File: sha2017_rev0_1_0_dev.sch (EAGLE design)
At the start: 195 parts, among them IC1 CP210X_USB_UART, IC2 AP7215, IC3 ESP32WROOM32, IC4 MCP73833, IC5 FXL6408, IC6 CPT112, Q1 MOSFET-PCHANNEL, Q2 MMBT2222A, Q3 MMBT2222A, Q4 MMBT2222A, Q5 MMBT2222A, Q6 SI1304 BDL, Q7 MMBT2222A, Q8 MOSFET-PCHANNEL, T1 SI2301DS, X1 JST-PH3, X2 2908-05WB-MG

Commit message: fixed designators
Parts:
- removed SJ3: JUMPER-PAD-2-NC_BY_TRACE, SparkFun-Passives:JUMPER-PAD-2-NC_BY_TRACE
- removed U$26, U$27, U$28: VIA, badge:VIA
- added $$U$1, $$U$2, $$U$3: VIA, badge:VIA
- added SJ1: JUMPER-PAD-2-NC_BY_TRACE, SparkFun-Passives:JUMPER-PAD-2-NC_BY_TRACE
- C10: PARTNO (none) -> GRM188R71H104KA93D
- C12: value 4u7/16V -> 100n; device rcl:C-EUC0805 -> rcl:C-EUC0603; PARTNO GRM21BR61C475KA88K -> (none)
- C13: OC_FARNELL unknown -> (none); PARTNO (none) -> GRM188R71H104KA93D
- C15: value 4u7/16V -> 100n; device rcl:C-EUC0805 -> rcl:C-EUC0603; OC_FARNELL (none) -> unknown; PARTNO GRM21BR61C475KA88K -> (none)
- C16, C29: value 1u -> 4u7/16V; device rcl:C-EUC0603 -> rcl:C-EUC0805; PARTNO GRM188R61E105KA12D -> GRM21BR61C475KA88K
- C19: value 100n -> 4u7/16V; device rcl:C-EUC0603 -> rcl:C-EUC0805; PARTNO GRM188R71H104KA93D -> GRM21BR61C475KA88K
- C20, C30: value 10uF -> 1u; device rcl:C-EUC0805K -> rcl:C-EUC0603; PARTNO (none) -> GRM188R61E105KA12D
- C21: value 100nF -> 100n; device rcl:C-EUC0402K -> rcl:C-EUC0603; PARTNO (none) -> GRM188R71H104KA93D
- C22, C32: value 1u -> 10uF; device rcl:C-EUC0603 -> rcl:C-EUC0805K; PARTNO GRM188R61E105KA12D -> (none)
- C23: value 4u7/16V -> 100nF; device rcl:C-EUC0805 -> rcl:C-EUC0402K; PARTNO GRM21BR61C475KA88K -> (none)
- C24, C35: value 100n -> 1u; PARTNO GRM188R71H104KA93D -> GRM188R61E105KA12D
- C25: value (none) -> 4u7/16V; device rcl:C-EUC0603 -> rcl:C-EUC0805; OC_FARNELL unknown -> (none); PARTNO (none) -> GRM21BR61C475KA88K
- C26, C37: value (none) -> 100n; OC_FARNELL unknown -> (none); PARTNO (none) -> GRM188R71H104KA93D
- C27: value 4u7/16V -> (none); device rcl:C-EUC0805 -> rcl:C-EUC0603; OC_FARNELL (none) -> unknown; PARTNO GRM21BR61C475KA88K -> (none)
- C28: value 1u -> (none); OC_FARNELL (none) -> unknown; PARTNO GRM188R61E105KA12D -> (none)
- C3: value 4u7/16V -> 100n; device 00ralf:C0603-DASHES -> rcl:C-EUC0603
- C36: value 4u7/16V -> 1u; device 00ralf:C0603-DASHES -> rcl:C-EUC0603; PARTNO (none) -> GRM188R61E105KA12D
- C38: value 100n -> 4u7/16V; device rcl:C-EUC0603 -> 00ralf:C0603-DASHES; PARTNO GRM188R71H104KA93D -> (none)
- C39: value 100n -> (none); OC_FARNELL (none) -> unknown; PARTNO GRM188R71H104KA93D -> (none)
- C4: value 100n -> 4u7/16V; device rcl:C-EUC0603 -> 00ralf:C0603-DASHES
- C7: value 4u7/16V -> 100n; device rcl:C-EUC0805 -> rcl:C-EUC0603; PARTNO GRM21BR61C475KA88K -> GRM188R71H104KA93D
- C8: value 100n -> 4u7/16V; device rcl:C-EUC0603 -> rcl:C-EUC0805; OC_FARNELL unknown -> (none); PARTNO (none) -> GRM21BR61C475KA88K
- C9: OC_FARNELL (none) -> unknown; PARTNO GRM188R71H104KA93D -> (none)
- D2: PARTNO (none) -> BAT20JFILM
- D3: value Yellow -> NSVR0320MW2T1G; device SparkFun-LED:LED0603 -> SparkFun-DiscreteSemi:BAT20JFILM
- D4: value RED -> Yellow
- D5: value green -> RED
- D6: value NSVR0320MW2T1G -> green; device SparkFun-DiscreteSemi:BAT20JFILM -> SparkFun-LED:LED0603; PARTNO BAT20JFILM -> (none)
- R1: value 10R -> 10k
- R10: device rcl:R-EU_R0603 -> 00ralf:R0603-DASHES; PARTNO ERJ-3GEYJ103V -> (none)
- R11, R9: value 1k -> 10k; device rcl:R-EU_R0603 -> 00ralf:R0603-DASHES; PARTNO ERJ-3GEYJ102V -> (none)
- R12, R14: value 10k -> 1k; PARTNO ERJ-3GEYJ103V -> ERJ-3GEYJ102V
- R15: value 5R -> 10k; device 00ralf:R0603-DASHES -> rcl:R-EU_R0603; PARTNO ERJ-3GEYJ5R1V -> ERJ-3GEYJ103V
- R16: value 100k -> 10k; PARTNO (none) -> ERJ-3GEYJ103V
- R17, R5: value 220k -> 10k; device rcl:R-EU_R0603 -> 00ralf:R0603-DASHES
- R18: OC_FARNELL unknown -> (none)
- R19: value 470R -> 5R; device rcl:R-EU_R0603 -> 00ralf:R0603-DASHES; OC_FARNELL unknown -> (none); PARTNO ERJ-3GEYJ103V -> ERJ-3GEYJ5R1V
- R2: value 1k -> 10R; device rcl:R-EU_R0603 -> 00ralf:R0603-DASHES; PARTNO ERJ-3GEYJ102V -> (none)
- R20: value 470R -> 100k; OC_FARNELL unknown -> (none); PARTNO ERJ-3GEYJ103V -> (none)
- R21, R7: value 10k -> 220k; device 00ralf:R0603-DASHES -> rcl:R-EU_R0603
- R22, R33: device 00ralf:R0603-DASHES -> rcl:R-EU_R0603; OC_FARNELL (none) -> unknown; PARTNO (none) -> ERJ-3GEYJ103V
- R23: value 2.2k -> 470R; OC_FARNELL (none) -> unknown; PARTNO (none) -> ERJ-3GEYJ103V
- R24: value 1k -> 470R; OC_FARNELL (none) -> unknown; PARTNO (none) -> ERJ-3GEYJ103V
- R25: value 100k -> 10k; device rcl:R-EU_R0603 -> 00ralf:R0603-DASHES; PARTNO CRCW0603100KFKEA -> (none)
- R26: value 150k -> 10k; device rcl:R-EU_R0603 -> 00ralf:R0603-DASHES
- R27: device rcl:R-EU_R0603 -> 00ralf:R0603-DASHES; OC_FARNELL unknown -> (none); PARTNO ERJ-3GEYJ103V -> (none)
- R28: value 1k -> 10k; device rcl:R-EU_R0603 -> 00ralf:R0603-DASHES
- R29: value 10k -> 2.2k; device 00ralf:R0603-DASHES -> rcl:R-EU_R0603
- R3: value 10k -> 1k; PARTNO (none) -> ERJ-3GEYJ102V
- R30, R34: value 10k -> 1k; device 00ralf:R0603-DASHES -> rcl:R-EU_R0603
- R31: value 10k -> 100k; device 00ralf:R0603-DASHES -> rcl:R-EU_R0603; PARTNO (none) -> CRCW0603100KFKEA
- R32: value 10k -> 150k; device 00ralf:R0603-DASHES -> rcl:R-EU_R0603
- R4: value 100k -> 10k
- R6: value 10k -> 100k; device 00ralf:R0603-DASHES -> rcl:R-EU_R0603
- X1: value JST-PH3 -> 2908-05WB-MG; device badge:JST-PH3 -> con-3m:2908-05WB-MG; PARTNO (none) -> 2908-05WB-MG
- X2: value 2908-05WB-MG -> (none); device con-3m:2908-05WB-MG -> EAGLE-BOARD-TO-BOARD_CONNECTORS-rev16c:610X12243021; PARTNO 2908-05WB-MG -> (none)
- X3: value (none) -> JST-PH3; device EAGLE-BOARD-TO-BOARD_CONNECTORS-rev16c:610X12243021 -> badge:JST-PH3
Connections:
- net +3V3: now also C11.1, C16.1, C21.1, C25.1, C26.1, C29.1, C36.1, C6.1, R1.2, R16.2, R17.2, R22.1, R23.1, R24.1, R25.2, R26.2, R31.1, R33.1, R5.2, R8.2; no longer C14.1, C17.1, C23.1, C24.1, C27.1, C34.1, C37.1, C38.1, R13.2, R18.1, R19.1, R20.1, R22.2, R25.1, R27.1, R29.2, R30.2, R31.2, R32.2, R33.2
- net +5V: now also C10.1, C22.2, C23.2, C8.1, D3.A, R4.2, R7.2; no longer C20.2, C21.2, C7.1, C9.1, D2.A, R3.2, R5.2
- net 3V3_SWITCHED: now also C37.1, C38.1, X1.VCC, X2.1; no longer C35.1, C36.1, X2.VCC, X3.1
- net ESP32_!RESET: now also R22.2; no longer R18.2
- net ESP32_FLASH: now also D2.C, R16.1; no longer D9.C, R13.1
- net ESP32_RX: now also D4.C; no longer D3.C
- net ESP32_TX: now also D5.C; no longer D4.C
- net EXTIO-0: now also X2.10; no longer X3.10
- net EXTIO-1: now also X2.9; no longer X3.9
- net EXTIO-2: now also X2.8; no longer X3.8
- net EXTIO-3: now also X2.4; no longer X3.4
- net EXTIO-4: now also X2.3; no longer X3.3
- net EXTIO-5: now also X2.2; no longer X3.2
- net GND: now also $$U$1.P$1, $$U$2.P$1, $$U$3.P$1, C10.2, C12.1, C16.2, C21.2, C22.1, C23.1, C25.2, C26.2, C27.1, C29.2, C3.1, C34.1, C35.1, C4.2, D7.C, R19.2, R20.1, R29.1, R32.1, R6.1, X1.GND, X1.SHIELD@2, X1.SHIELD@3, X1.SHIELD@4, X2.12, X32.1; no longer C10.1, C12.2, C16.1, C21.1, C23.2, C24.2, C25.1, C26.1, C27.2, C29.1, C3.2, C34.2, C35.2, C4.1, D5.C, R15.2, R16.1, R23.1, R26.1, R3.1, U$26.P$1, U$27.P$1, U$28.P$1, X12.1, X2.GND, X2.SHIELD@2, X2.SHIELD@3, X2.SHIELD@4, X3.12
- net I2C_SCL: now also R24.2, X2.7; no longer R20.2, X3.7
- net I2C_SDA: now also R23.2, X2.6; no longer R19.2, X3.6
- net N$10: now also R15.1; no longer R12.1
- net N$11: now also R18.1; no longer R14.1
- net N$13: now also R15.2; no longer R12.2
- net N$14: now also R18.2; no longer R14.2
- net N$15: now also R27.2; no longer R21.2
- net N$17: now also R28.1; no longer R22.1
- net N$18: now also R2.1; no longer R1.1
- net N$20: now also SJ2.2, X1.DO; no longer SJ3.2, X2.DO
- net N$22: now also C24.1, D7.A, D8.C; no longer C22.1, D6.A, D7.C
- net N$23: now also C24.2, D9.A; no longer C22.2, D8.A
- net N$26: now also D6.A, R12.1; no longer D5.A, R9.1
- net N$27: now also D4.A, R3.1; no longer D3.A, R2.1
- net N$28: now also D5.A, R14.1; no longer D4.A, R11.1
- net N$42: now also C27.2; no longer C25.2
- net N$43: now also C28.2; no longer C26.2
- net N$45: now also R11.1; no longer R8.1
- net N$46: now also R29.2; no longer R23.2
- net N$47: now also R30.2; no longer R24.2
- net N$48: now also R30.1, R32.2, X31.1; no longer R24.1, R26.2, X11.1
- net N$49: now also C32.2, X33.1; no longer C30.2, X13.1
- net N$52: now also R10.2; no longer R7.2
- net N$53: now also R9.1; no longer R6.1
- net N$59: now also R33.2; no longer R27.2
- net N$61: now also R34.1; no longer R28.1
- net N$8: now also R13.2; no longer R10.2
- net PREVGH: now also C30.2, D9.C; no longer C28.2, D8.C
- net PREVGL: now also C34.2, D8.A; no longer C32.2, D7.A
- net RESE: now also R19.1; no longer R15.1
- net SD_CD: now also R31.2, X1.SHIELD@1; no longer R25.2, X2.SHIELD@1
- net SD_CLK: now also R25.1, X1.SCK; no longer R32.1, X2.SCK
- net SD_CMD: now also R8.1, X1.DI; no longer R31.1, X2.DI
- net SD_DATA0: now also D2.A, R5.1, SJ2.1; no longer D9.A, R33.1, SJ3.1
- net SD_DATA1: now also R1.1, X1.RSV; no longer R34.1, X2.RSV
- net SD_DATA2: now also SJ1.1; no longer SJ2.1
- net SD_DATA2_OUT: now also R26.1, SJ1.2, X1.NC; no longer R29.1, SJ2.2, X2.NC
- net SD_DATA3: now also R17.1, X1.CS; no longer R30.1, X2.CS
- net VBAT: now also R21.2; no longer R17.2
- net VBAT_SENSE: now also C15.1, R20.2, R21.1; no longer C13.1, R16.2, R17.1
- net VCC: now also C13.1, C14.1, C17.1, D3.C, R2.2, R9.2; no longer C11.1, C12.1, C15.1, D2.C, R1.2, R6.2
- net VCOM: now also C35.2; no longer C33.2
- net VDD: now also C7.1, R12.2, R13.1, R14.2, R3.2; no longer C6.1, R10.1, R11.2, R2.2, R9.2
- net VGH: now also C20.2; no longer C18.2
- net VGL: now also C18.2; no longer C16.2
- net VIBRATOR: now also R11.2; no longer R8.2
- net VSH: now also C31.2; no longer C29.2
- net VSL: now also C33.2; no longer C31.2
- net VUSB_SENSE: now also C9.1, R6.2, R7.1; no longer C8.1, R4.2, R5.1
- net WS2812_DATA_OUT: now also X2.5; no longer X3.5
- net WS2812_POWER: now also C12.2, C3.2, C4.1, X2.11; no longer C10.2, C3.1, C4.2, X3.11
- net WS2812_POWER_EN: now also R10.1, R27.1; no longer R21.1, R7.1

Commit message: some small fixes
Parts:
- renumbered J1 to X4
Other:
- note added: "Port Expander"
- note added: "Spezial Vias with thermals (hack)"
- note added: "Touch Controller"
- moved on the sheet: C39, IC5, R23, R24, R33, TP102, TP109, TP111, TP113, TP114, TP115, TP116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

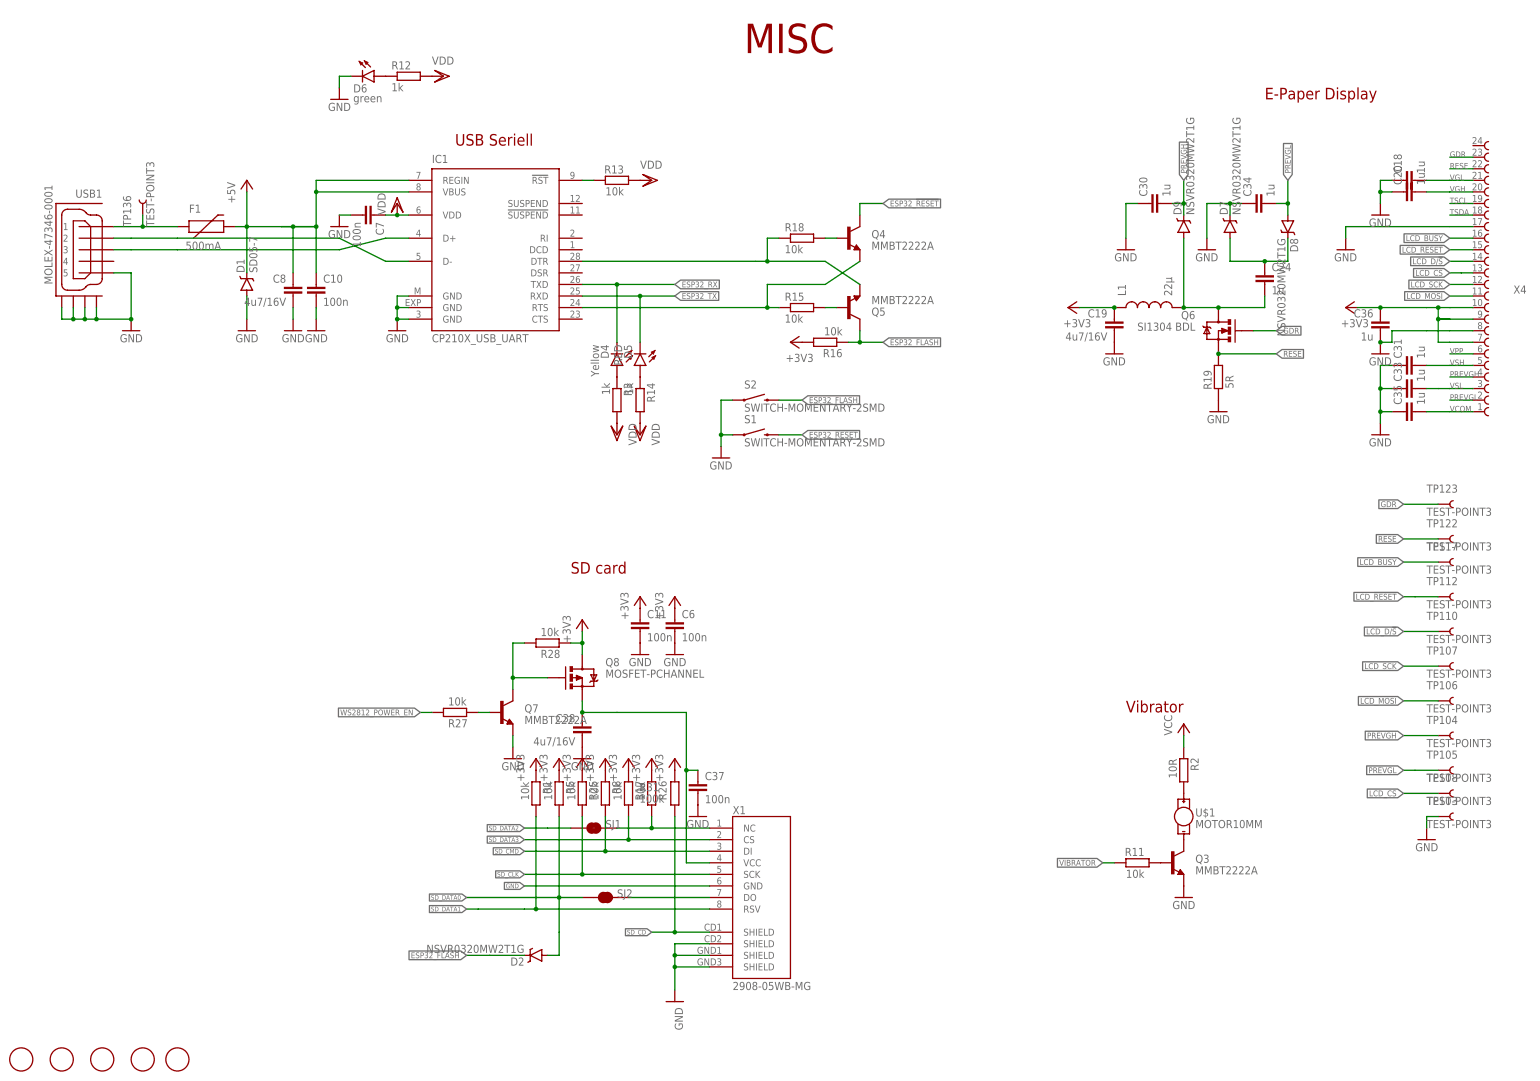
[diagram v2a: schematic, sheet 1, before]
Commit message: cleanup an Testpoint marking
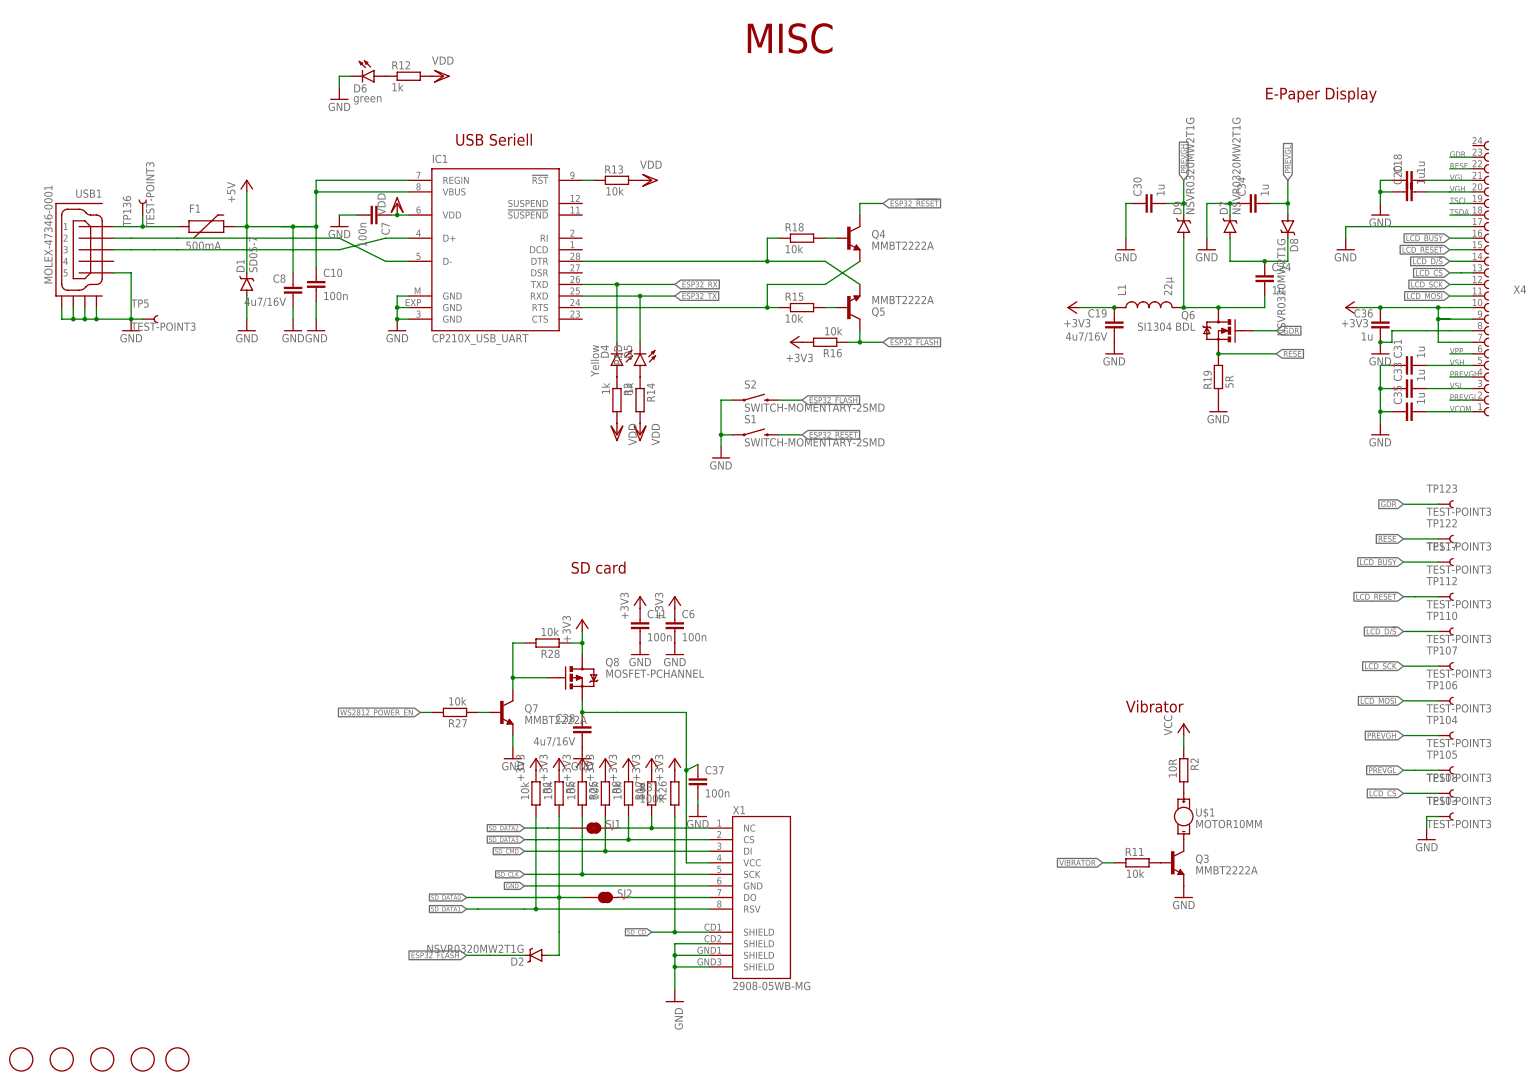
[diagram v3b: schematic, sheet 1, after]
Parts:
- added TP5: TEST-POINT3, SparkFun-Passives:TEST-POINT3
- $$U$1, $$U$2, $$U$3, $$U$7, $$U$8, $$U$9, FD1, FD2, FD3, FD4, FD5, TB100, TB101, TB102, TB103, TB104, TP1, TP100, TP101, TP102, TP103, TP104, TP105, TP106, TP107, TP108, TP109, TP110, TP111, TP112, TP113, TP114, TP115, TP116, TP117, TP118, TP119, TP120, TP121, TP122, TP123, TP124, TP125, TP126, TP127, TP128, TP129, TP130, TP131, TP132, TP133, TP134, TP135, TP136, TP137, TP138, TP139, TP2, U$10, U$11, U$12, U$13, U$14, U$15, U$16, U$17, U$18, U$19, U$2, U$20, U$21, U$22, U$23, U$24, U$25, U$3, U$4, U$5, U$6: PARTNO (none) -> NAP
- C1, C12, C15, C2, C3, C5, C9: device rcl:C-EUC0603 -> sha2017_rev0_1_0_dev:C0603-DASHES; PARTNO (none) -> GRM188R71H104KA93D
- C10, C11, C13, C18, C20, C21, C24, C26, C30, C31, C33, C34, C35, C36, C37, C39, C40, C6, C7: device rcl:C-EUC0603 -> sha2017_rev0_1_0_dev:C0603-DASHES
- C22, C32: value 10uF -> 10u
- C23: value 100nF -> 100n; device rcl:C-EUC0402K -> sha2017_rev0_1_0_dev:C0603-DASHES; PARTNO (none) -> GRM188R71H104KA93D
- C27, C28: value (none) -> 100n; device rcl:C-EUC0603 -> sha2017_rev0_1_0_dev:C0603-DASHES
- D100, D101, D102, D103, D104: PARTNO (none) -> WS2812B
- D3: PARTNO (none) -> BAT20JFILM
- F2: PARTNO (none) -> 0ZCJ0025FF2E
- Q2, Q3, Q7: PARTNO (none) -> BC817-25,215
- R1, R10, R11, R27, R28, R5, R8, R9: PARTNO (none) -> ERJ-3GEYJ103V
- R12, R13, R14, R15, R16, R18, R21, R22, R23, R24, R29, R3, R31, R32, R33, R7: device rcl:R-EU_R0603 -> sha2017_rev0_1_0_dev:R0603-DASHES
- R17, R25, R26: device 00ralf:R0603-DASHES -> sha2017_rev0_1_0_dev:R0603-DASHES; PARTNO (none) -> ERJ-3GEYJ103V
- R19: device 00ralf:R0603-DASHES -> sha2017_rev0_1_0_dev:R0603-DASHES
- R20, R6: device rcl:R-EU_R0603 -> sha2017_rev0_1_0_dev:R0603-DASHES; PARTNO (none) -> CRCW0603100KFKEA
- R30, R34: device rcl:R-EU_R0603 -> sha2017_rev0_1_0_dev:R0603-DASHES; PARTNO (none) -> ERJ-3GEYJ102V
- R4: device rcl:R-EU_R0603 -> sha2017_rev0_1_0_dev:R0603-DASHES; PARTNO (none) -> ERJ-3GEYJ103V
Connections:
- net N$12 renamed SD1
- net N$3 renamed SD2
- net N$4 renamed SD3
- net N$6 renamed CND
- net N$7 renamed CLK
- net N$9 renamed CD0
- net GND: now also TP5.1
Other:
- moved on the sheet: C10, C15, C27, C28, C30, C34, C37, C7, C9
